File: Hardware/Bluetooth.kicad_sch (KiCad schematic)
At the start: 1 part, among them J6 HC05_Breakout

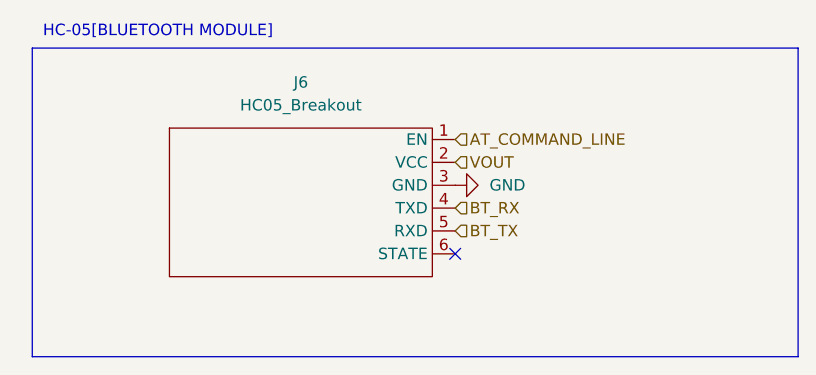
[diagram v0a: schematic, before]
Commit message: Schematic updated with buck and motor driver breakout boards
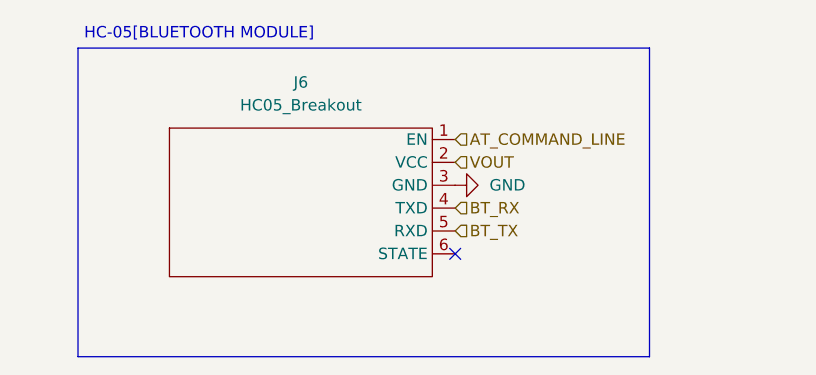
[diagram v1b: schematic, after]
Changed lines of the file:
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@@
 	(paper "A4")
 	(rectangle
-		(start 101.6 72.39)
-		(end 186.69 106.68)
+		(start 106.68 72.39)
+		(end 170.18 106.68)
 		(stroke
 			(width 0)
@@
 	(text "HC-05[BLUETOOTH MODULE]"
 		(exclude_from_sim no)
-		(at 115.57 70.612 0)
+		(at 120.142 70.866 0)
 		(effects
 			(font
